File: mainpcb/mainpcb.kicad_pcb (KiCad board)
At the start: 2 copper layers, 146 x 116.9 mm, 38 parts, among them J1 Conn_01x05_Female, J2 Conn_01x05_Female, J3 Conn_01x04_Female, SW1 SW_PUSH, SW10 SW_PUSH, SW11 SW_PUSH, SW12 SW_PUSH, SW13 SW_PUSH, SW14 SW_PUSH, SW15 SW_PUSH, SW16 SW_PUSH, SW17 SW_PUSH, SW18 SW_PUSH, SW19 SW_PUSH, SW2 SW_PUSH, SW20 SW_PUSH, SW21 SW_PUSH, SW3 SW_PUSH, SW4 SW_PUSH, SW5 SW_PUSH, SW6 SW_PUSH, SW7 SW_PUSH, SW8 SW_PUSH, SW9 SW_PUSH, U1 MCP23017_SS, U2 MCP23017_SS, U3 MCP23017_SS, U4 MCP23017_SS

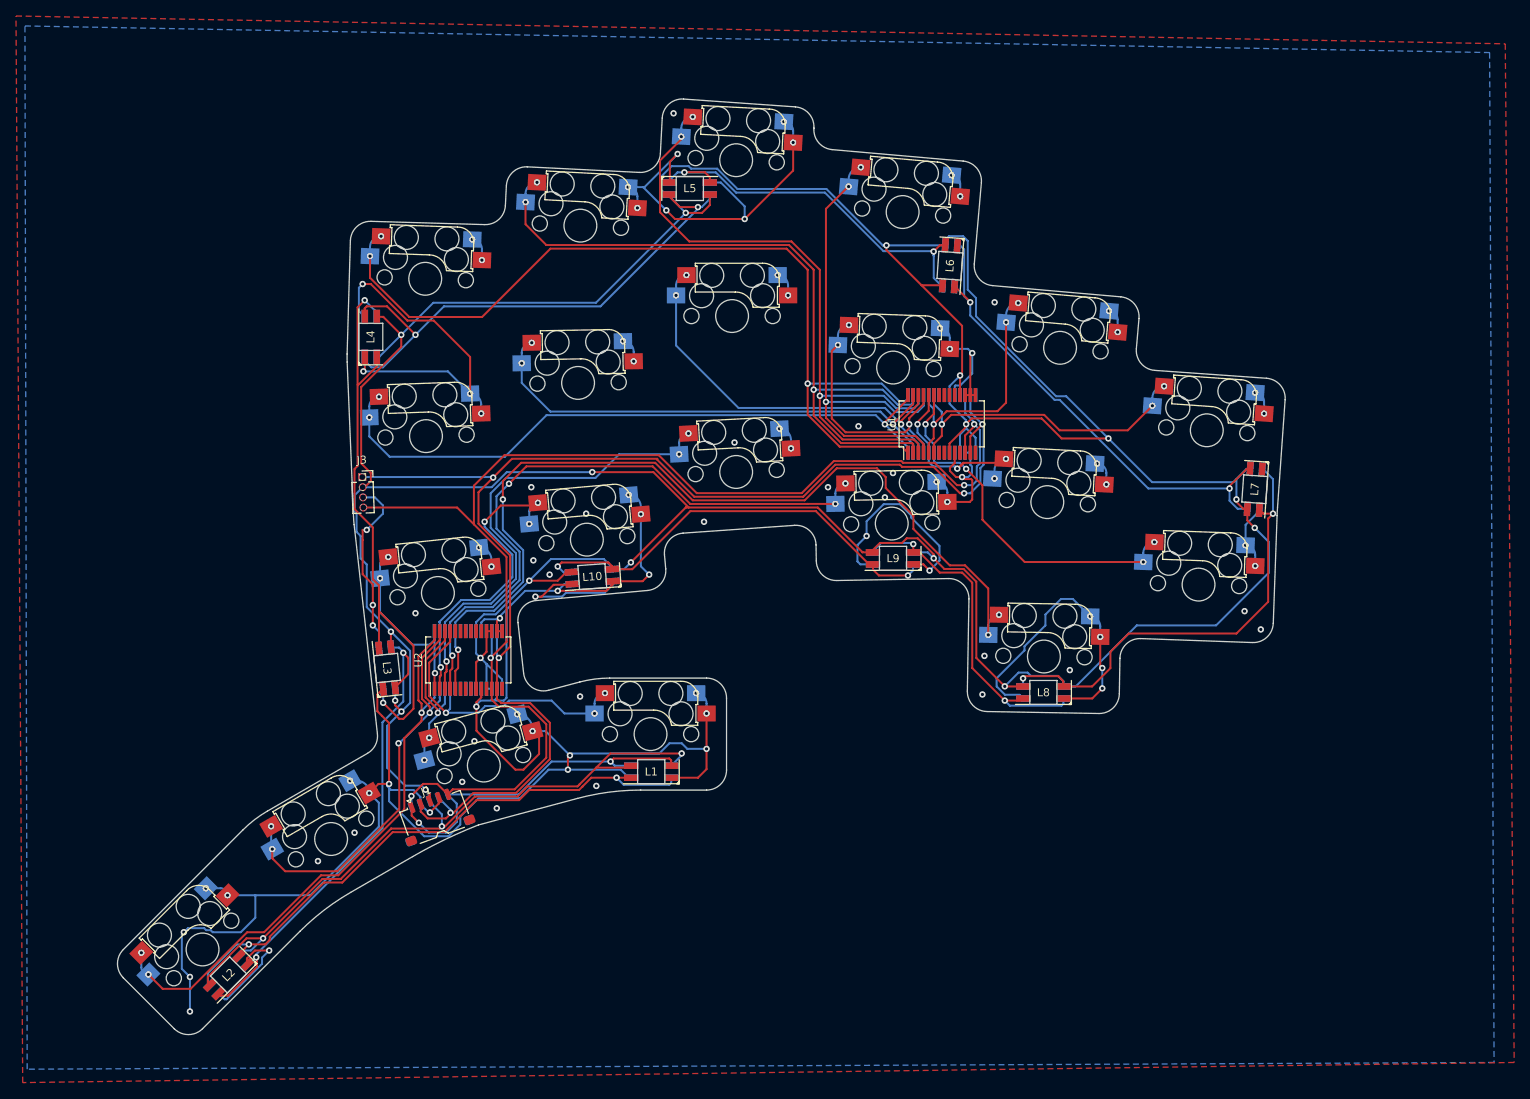
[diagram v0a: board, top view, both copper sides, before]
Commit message: key-matrix using single mcp23017
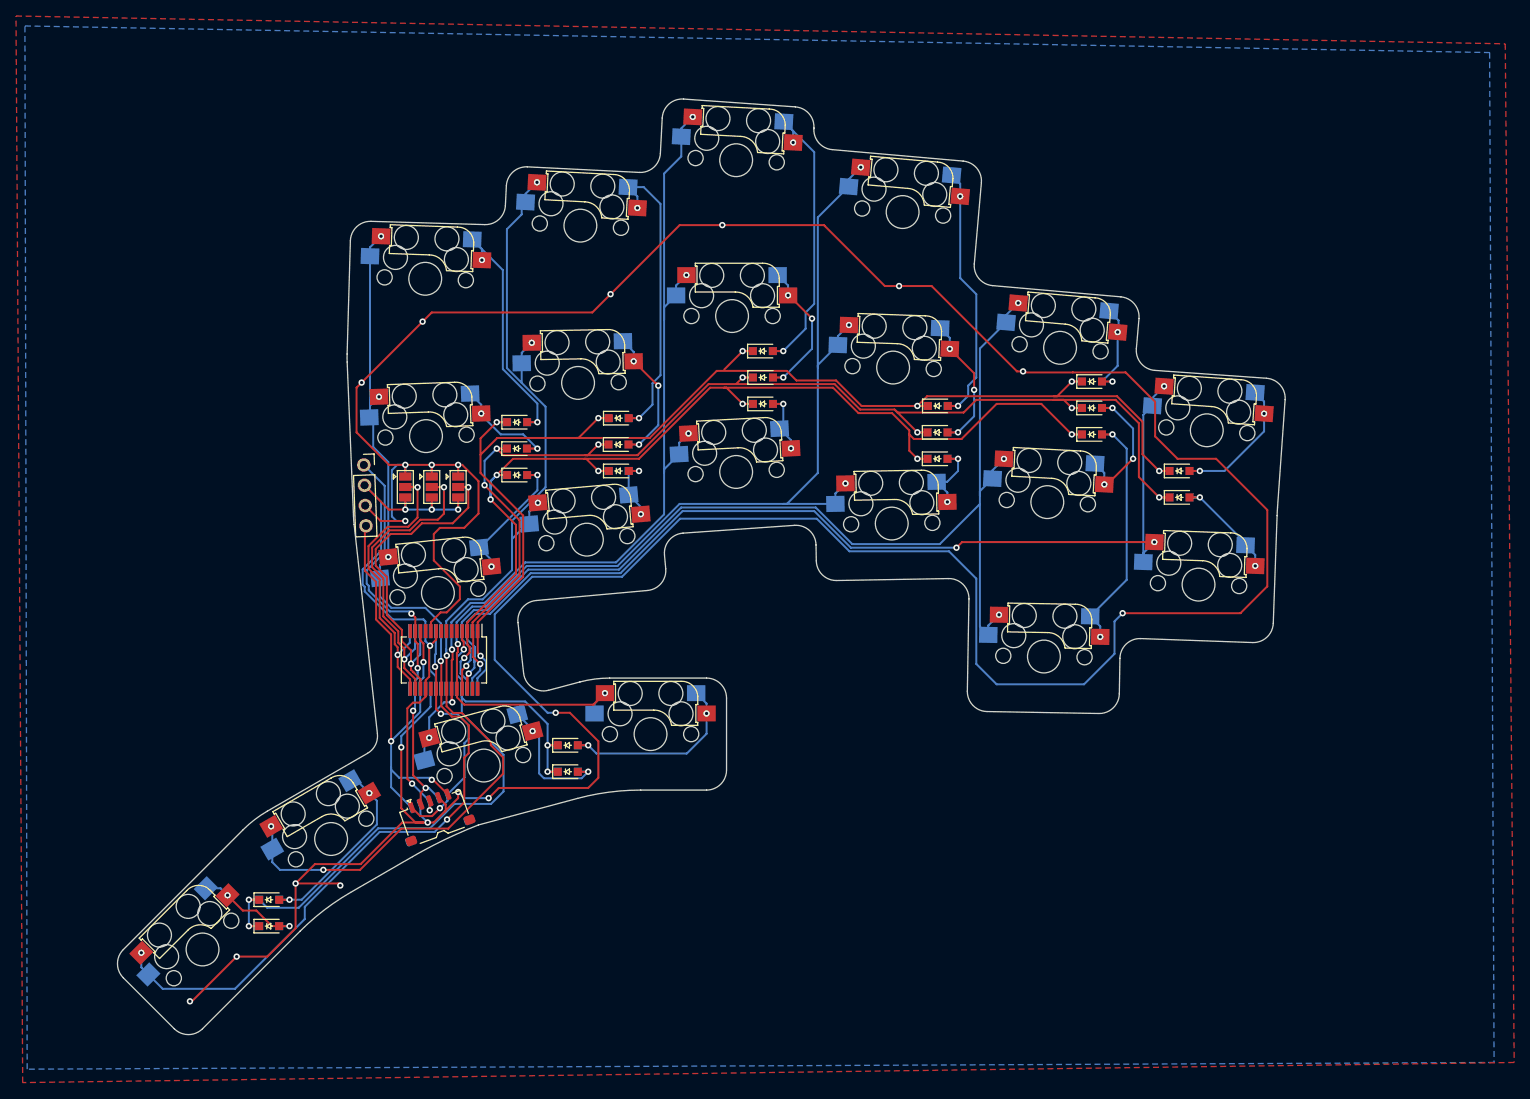
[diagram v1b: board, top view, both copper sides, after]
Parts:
- removed L1, L10, L2, L3, L4, L5, L6, L7, L8, L9: YS-SK6812MINI, mammoth:YS-SK6812MINI-E-underglow_R
- removed U3, U4: MCP23017_SS, Package_SO:SSOP-28_5.3x10.2mm_P0.65mm
- added D1: D, mammoth:D_SOD-323_HandSoldering_rev, F.Cu at (99.6, 72.4)
- added D10: D, mammoth:D_SOD-323_HandSoldering_rev, F.Cu at (152.1, 73.7)
- added D11: D, mammoth:D_SOD-323_HandSoldering_rev, F.Cu at (171.4, 70.6)
- added D12: D, mammoth:D_SOD-323_HandSoldering_rev, F.Cu at (182.4, 81.8)
- added D13: D, mammoth:D_SOD-323_HandSoldering_rev, F.Cu at (99.6, 79.0)
- added D14: D, mammoth:D_SOD-323_HandSoldering_rev, F.Cu at (112.3, 78.5)
- added D15: D, mammoth:D_SOD-323_HandSoldering_rev, F.Cu at (130.3, 70.1)
- added D16: D, mammoth:D_SOD-323_HandSoldering_rev, F.Cu at (152.1, 77.0)
- added D17: D, mammoth:D_SOD-323_HandSoldering_rev, F.Cu at (171.4, 73.9)
- added D18: D, mammoth:D_SOD-323_HandSoldering_rev, F.Cu at (68.6, 135.4)
- added D19: D, mammoth:D_SOD-323_HandSoldering_rev, F.Cu at (68.6, 132.1)
- added D2: D, mammoth:D_SOD-323_HandSoldering_rev, F.Cu at (112.3, 71.9)
- added D20: D, mammoth:D_SOD-323_HandSoldering_rev, F.Cu at (105.9, 116.1)
- added D21: D, mammoth:D_SOD-323_HandSoldering_rev, F.Cu at (105.9, 112.8)
- added D3: D, mammoth:D_SOD-323_HandSoldering_rev, F.Cu at (130.3, 63.5)
- added D4: D, mammoth:D_SOD-323_HandSoldering_rev, F.Cu at (152.1, 70.4)
- added D5: D, mammoth:D_SOD-323_HandSoldering_rev, F.Cu at (171.4, 67.3)
- added D6: D, mammoth:D_SOD-323_HandSoldering_rev, F.Cu at (182.4, 78.5)
- added D7: D, mammoth:D_SOD-323_HandSoldering_rev, F.Cu at (99.5, 75.7)
- added D8: D, mammoth:D_SOD-323_HandSoldering_rev, F.Cu at (112.2, 75.2)
- added D9: D, mammoth:D_SOD-323_HandSoldering_rev, F.Cu at (130.3, 66.8)
- added JP1: SolderJumper_3_Open, Jumper:SolderJumper-3_P1.3mm_Open_Pad1.0x1.5mm, F.Cu at (85.6, 80.5)
- added JP2: SolderJumper_3_Open, Jumper:SolderJumper-3_P1.3mm_Open_Pad1.0x1.5mm, F.Cu at (88.9, 80.5)
- added JP3: SolderJumper_3_Open, Jumper:SolderJumper-3_P1.3mm_Open_Pad1.0x1.5mm, F.Cu at (92.2, 80.5)
- added JP4: SolderJumper_3_Open, Jumper:SolderJumper-3_P1.3mm_Open_Pad1.0x1.5mm, B.Cu at (85.6, 80.5)
- added JP5: SolderJumper_3_Open, Jumper:SolderJumper-3_P1.3mm_Open_Pad1.0x1.5mm, B.Cu at (88.9, 80.5)
- added JP6: SolderJumper_3_Open, Jumper:SolderJumper-3_P1.3mm_Open_Pad1.0x1.5mm, B.Cu at (92.2, 80.5)
- J3: footprint Connector_PinSocket_1.27mm:PinSocket_1x04_P1.27mm_Vertical -> Connector_PinSocket_2.54mm:PinSocket_1x04_P2.54mm_Vertical
- U2: moved to B.Cu
- moved U1 68.9 mm to (90.4, 102.1), turned to -90 degrees
- moved U2 3.09 mm to (90.4, 102.1)
- moved J3 1.52 mm to (80.4, 77.7)
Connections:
- J1 pad 1: LED_I -> int
- J2 pad 1: LED_I -> int
- SW1 pad 1: sw00 -> col0
- SW1 pad 2: GND -> Net-(SW1-Pad2)
- SW10 pad 1: sw13 -> col3
- SW10 pad 2: GND -> Net-(SW10-Pad2)
- SW11 pad 1: sw14 -> col4
- SW11 pad 2: GND -> Net-(SW11-Pad2)
- SW12 pad 1: sw15 -> col5
- SW12 pad 2: GND -> Net-(SW12-Pad2)
- SW13 pad 1: sw20 -> col0
- SW13 pad 2: GND -> Net-(D13-Pad2)
- SW14 pad 1: sw21 -> col1
- SW14 pad 2: GND -> Net-(D14-Pad2)
- SW15 pad 1: sw22 -> col2
- SW15 pad 2: GND -> Net-(D15-Pad2)
- SW16 pad 1: sw23 -> col3
- SW16 pad 2: GND -> Net-(D16-Pad2)
- SW17 pad 1: sw24 -> col4
- SW17 pad 2: GND -> Net-(D17-Pad2)
- SW18 pad 1: sw30 -> col0
- SW18 pad 2: GND -> Net-(SW18-Pad2)
- SW19 pad 1: sw31 -> col1
- SW19 pad 2: GND -> Net-(SW19-Pad2)
- SW2 pad 1: sw01 -> col1
- SW2 pad 2: GND -> Net-(SW2-Pad2)
- SW20 pad 1: sw32 -> col2
- SW20 pad 2: GND -> Net-(SW20-Pad2)
- SW21 pad 1: sw33 -> col3
- SW21 pad 2: GND -> Net-(SW21-Pad2)
- SW3 pad 1: sw02 -> col2
- SW3 pad 2: GND -> Net-(SW3-Pad2)
- SW4 pad 1: sw03 -> col3
- SW4 pad 2: GND -> Net-(SW4-Pad2)
- SW5 pad 1: sw04 -> col4
- SW5 pad 2: GND -> Net-(SW5-Pad2)
- SW6 pad 1: sw05 -> col5
- SW6 pad 2: GND -> Net-(SW6-Pad2)
- SW7 pad 1: sw10 -> col0
- SW7 pad 2: GND -> Net-(SW7-Pad2)
- SW8 pad 1: sw11 -> col1
- SW8 pad 2: GND -> Net-(SW8-Pad2)
- SW9 pad 1: sw12 -> col2
- SW9 pad 2: GND -> Net-(SW9-Pad2)
- U1 pad 1: sw00 -> row0
- U1 pad 15: GND -> adr0
- U1 pad 16: GND -> adr1
- U1 pad 17: GND -> adr2
- U1 pad 2: sw01 -> row1
- U1 pad 20: unconnected-(U1-Pad20) -> int
- U1 pad 21: unconnected-(U1-Pad21) -> col0
- U1 pad 22: unconnected-(U1-Pad22) -> col1
- U1 pad 23: sw15 -> col2
- U1 pad 24: sw14 -> col3
- U1 pad 25: sw13 -> col4
- U1 pad 26: sw12 -> col5
- U1 pad 27: sw11 -> unconnected-(U1-Pad27)
- U1 pad 28: sw10 -> unconnected-(U1-Pad28)
- U1 pad 3: sw02 -> row2
- U1 pad 4: sw03 -> row3
- U1 pad 5: sw04 -> unconnected-(U1-Pad5)
- U1 pad 6: sw05 -> unconnected-(U1-Pad6)
- U2 pad 1: sw20 -> row0
- U2 pad 15: GND -> adr0
- U2 pad 16: GND -> adr1
- U2 pad 17: VDD -> adr2
- U2 pad 2: sw21 -> row1
- U2 pad 20: unconnected-(U2-Pad20) -> int
- U2 pad 21: unconnected-(U2-Pad21) -> col0
- U2 pad 22: unconnected-(U2-Pad22) -> col1
- U2 pad 23: unconnected-(U2-Pad23) -> col2
- U2 pad 24: unconnected-(U2-Pad24) -> col3
- U2 pad 25: sw33 -> col4
- U2 pad 26: sw32 -> col5
- U2 pad 27: sw31 -> unconnected-(U2-Pad27)
- U2 pad 28: sw30 -> unconnected-(U2-Pad28)
- U2 pad 3: sw22 -> row2
- U2 pad 4: sw23 -> row3
- U2 pad 5: sw24 -> unconnected-(U2-Pad5)
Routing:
- net VDD: track 603.7 -> 82.2 mm, vias 21 -> 6
- net row0: track 0.00 -> 162.7 mm, vias 0 -> 7
- net row1: track 0.00 -> 158.8 mm, vias 0 -> 8
- net col3: track 0.00 -> 141.8 mm, vias 0 -> 5
- net row2: track 0.00 -> 140.0 mm, vias 0 -> 7
- net col1: track 0.00 -> 137.0 mm, vias 0 -> 6
- net col4: track 0.00 -> 136.7 mm, vias 0 -> 4
- net col0: track 0.00 -> 135.5 mm, vias 0 -> 6
- net col5: track 0.00 -> 134.3 mm, vias 0 -> 4
- net SDA: track 169.7 -> 51.7 mm, vias 5 -> 4
- net col2: track 0.00 -> 117.6 mm, vias 0 -> 6
- net sw24: track 115.1 -> 0.00 mm, vias 4 -> 0
- net sw00: track 113.5 -> 0.00 mm, vias 3 -> 0
- net SCL: track 166.2 -> 61.7 mm, vias 4 -> 3
- net sw01: track 92.8 -> 0.00 mm, vias 3 -> 0
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
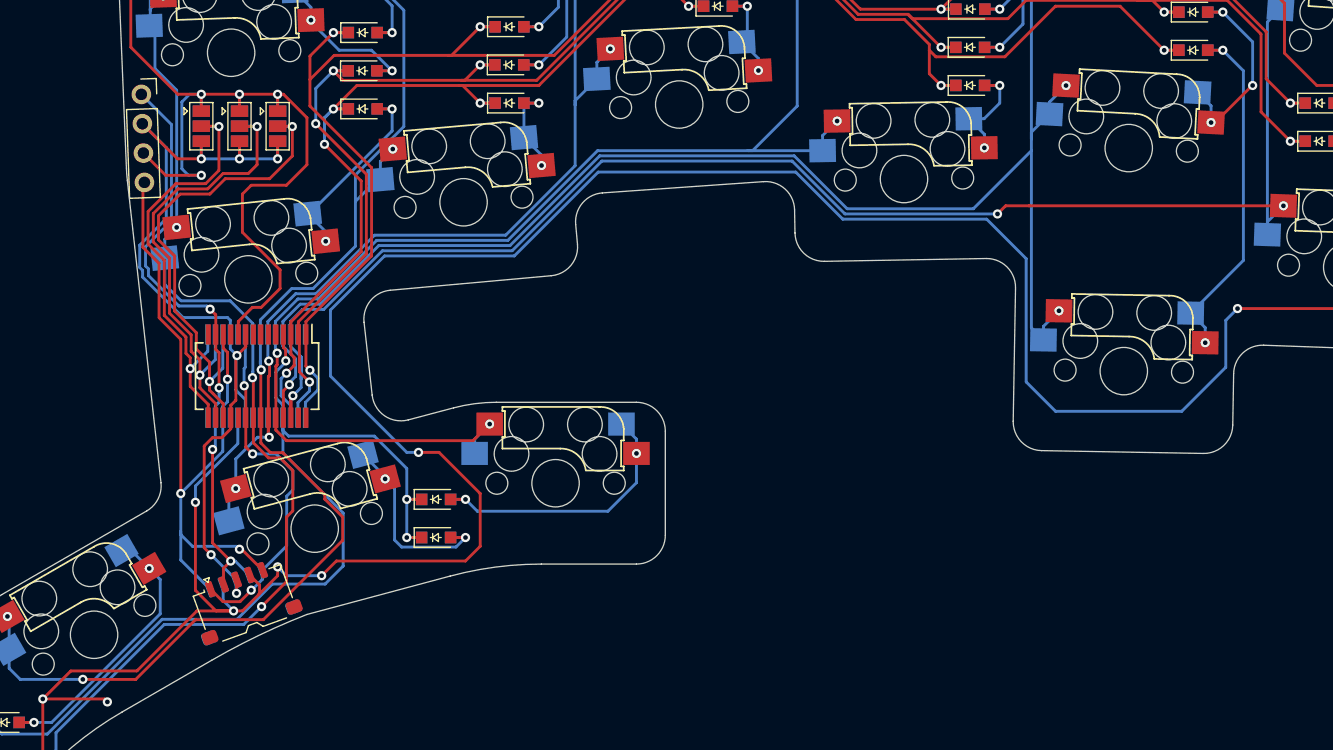
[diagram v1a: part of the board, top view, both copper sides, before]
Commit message: fix footprint
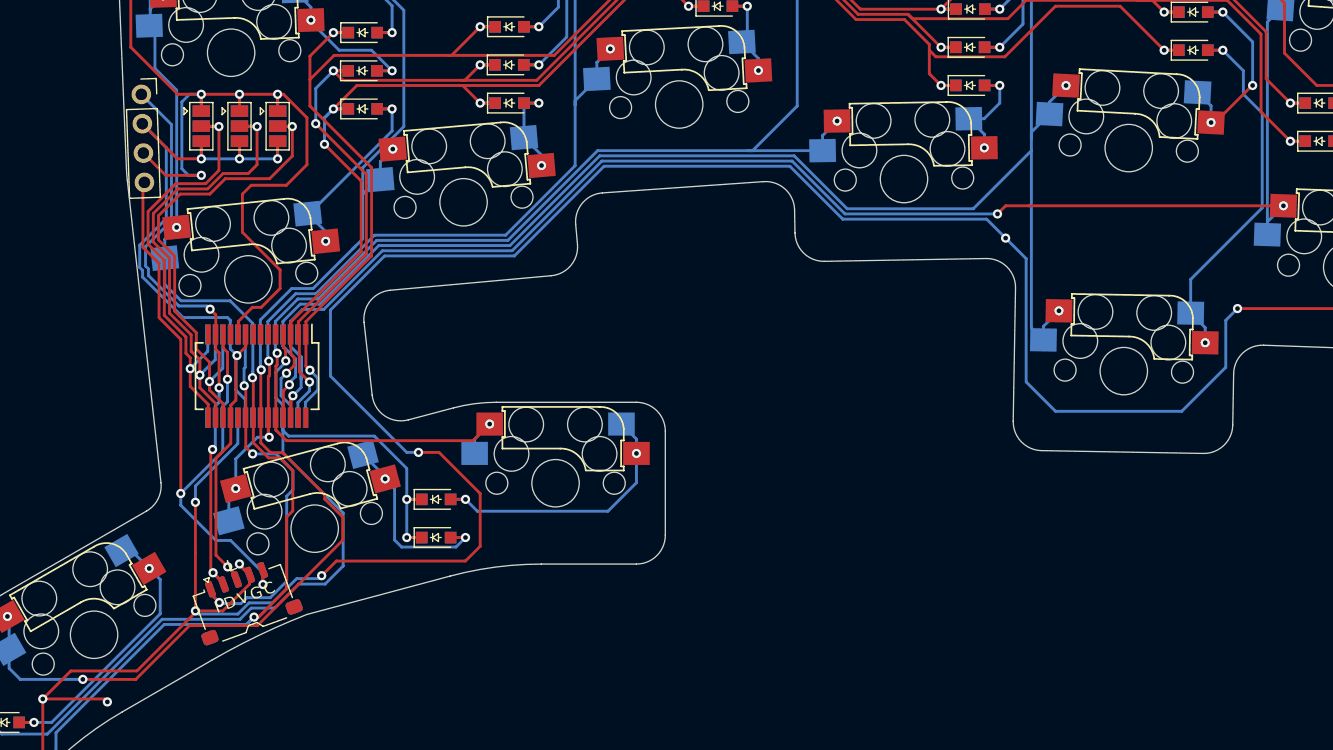
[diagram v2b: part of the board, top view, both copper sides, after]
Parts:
- removed J2: Conn_01x05_Female, mammoth:JST_ACH_BM05B-ACHSS-A-GAN-ETF_1x05-1MP_P1.20mm_Vertical
- J1: footprint mammoth:JST_ACH_BM05B-ACHSS-A-GAN-ETF_1x05-1MP_P1.20mm_Vertical -> mammoth:JST_ACH_BM05B-ACHSS-A-GAN-ETF_1x05-1MP_P1.20mm_Vertical_rev
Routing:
- net SCL: track 61.7 -> 56.6 mm
- net VDD: track 82.2 -> 79.2 mm, vias 6 -> 5
- net col0: track 135.5 -> 137.8 mm
- net int: track 31.4 -> 33.4 mm
- net GND: track 472.1 -> 473.7 mm, vias 20 -> 21
- net Net-(D17-Pad2): track 31.1 -> 32.4 mm
- net SDA: track 51.7 -> 50.4 mm

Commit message: revenge3
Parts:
- added G***: LOGO, mammoth:icon, F.Cu at (106.2, 55.4)
- added G***: LOGO, mammoth:icon, B.Cu at (106.2, 55.4)
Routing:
- net col1: track 136.6 -> 136.1 mm
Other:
- board text added: "0"
- board text added: "1"
- board text added: "2"
- board text added: "C"
- board text added: "D"
- board text added: "G"
- board text added: "V"

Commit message: revenge 4
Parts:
- removed the G*** at (106.2, 55.4) (x2)
- removed J3: Conn_01x04_Female, Connector_PinSocket_2.54mm:PinSocket_1x04_P2.54mm_Vertical
- added G***: LOGO, mammoth:mammoth, F.Cu at (107.2, 55.4)
- added G***: LOGO, mammoth:mammoth, B.Cu at (107.2, 55.4)
- D1, D10, D11, D12, D13, D14, D15, D16, D17, D18, D19, D2, D20, D21, D3, D4, D5, D6, D7, D8, D9: footprint mammoth:D_SOD-323_HandSoldering_rev -> mammoth:D3_SMD_v2
- moved D19 2.34 mm to (69.1, 129.8)
- moved D18 2.34 mm to (69.1, 133.1)
- moved D7 1.29 mm to (100.8, 75.7)
- moved D1 1.27 mm to (100.8, 72.4)
- moved D13 1.27 mm to (100.8, 79.0)
- moved D12 1.27 mm to (183.6, 81.8)
- moved D4 1.27 mm to (150.9, 70.4)
- moved D6 1.27 mm to (183.6, 78.5)
- moved D10 1.25 mm to (150.9, 73.7)
- moved D16 1.25 mm to (150.9, 77.0)
- moved D21 1.14 mm to (106.9, 113.3)
- moved D20 1.05 mm to (106.9, 116.3)
- moved D15 1.02 mm to (129.3, 70.1)
- moved D9 1.02 mm to (129.3, 66.8)
- moved D11 1.00 mm to (170.4, 70.6)
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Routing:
- net SCL: track 56.6 -> 28.5 mm, vias 3 -> 2
- net SDA: track 50.4 -> 23.7 mm, vias 4 -> 3
- net row1: track 158.8 -> 172.9 mm
- net row0: track 162.7 -> 174.4 mm
- net row2: track 140.0 -> 146.9 mm
- net row3: track 92.7 -> 97.4 mm
- net GND: track 473.7 -> 469.9 mm
- net Net-(D11-Pad2): track 17.7 -> 20.7 mm
- net col1: track 136.1 -> 138.2 mm
- net Net-(D20-Pad2): track 17.8 -> 19.9 mm
- net Net-(D6-Pad2): track 18.0 -> 20.0 mm
- net Net-(D18-Pad2): track 13.7 -> 15.3 mm
- net Net-(D4-Pad2): track 33.6 -> 35.1 mm
- net Net-(D10-Pad2): track 18.2 -> 19.7 mm
- net Net-(D16-Pad2): track 10.5 -> 11.9 mm
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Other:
- board text added: "STEP 2 REVENGE 4"
- board text removed: "C"
- board text removed: "D"
- board text removed: "G"
- board text removed: "V"
